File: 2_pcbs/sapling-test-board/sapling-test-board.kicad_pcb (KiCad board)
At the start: 2 copper layers, 10 parts, among them IC1 LED driver TLC59281DBQR, IC2 LED driver TLC59281DBQR, IC3 74HC138D, J1 Pin header BCS-112-L-D-PE, J2 UJC-HP-3-SMT-TR

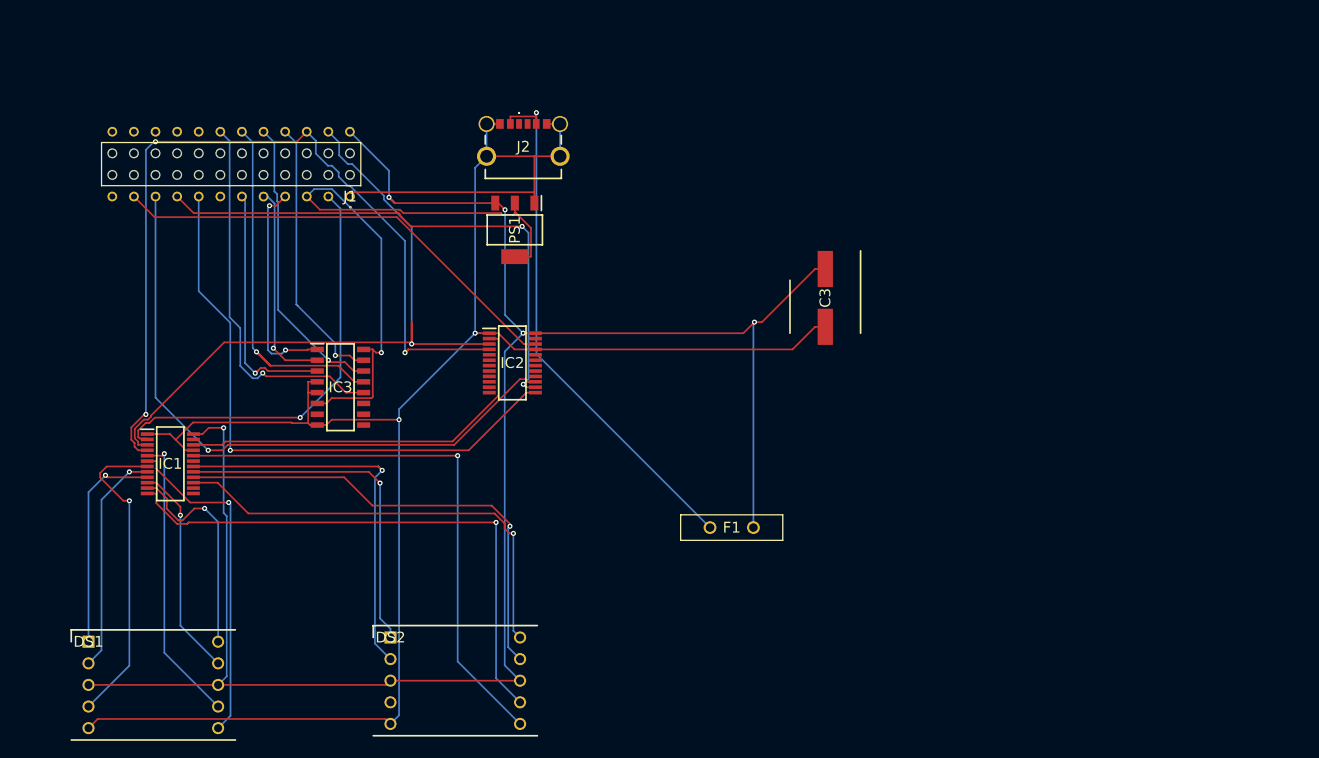
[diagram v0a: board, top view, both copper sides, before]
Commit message: Hand routed PCB
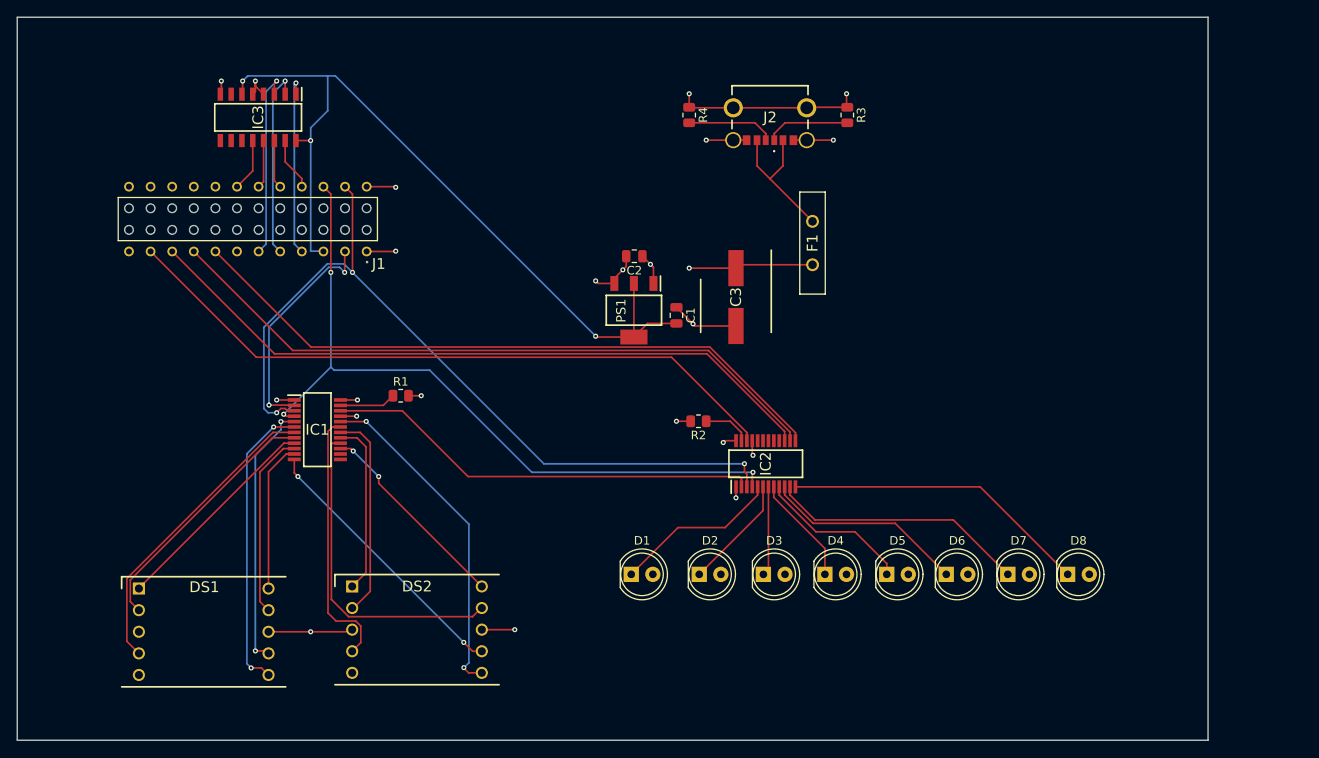
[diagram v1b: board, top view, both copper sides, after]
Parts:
- added C1: C, Capacitor_SMD:C_0805_2012Metric, F.Cu at (112.5, 55.0)
- added C2: C, Capacitor_SMD:C_0805_2012Metric, F.Cu at (107.5, 48.1)
- added D1: LED, LED_THT:LED_D5.0mm, F.Cu at (107.2, 85.5)
- added D2: LED, LED_THT:LED_D5.0mm, F.Cu at (115.2, 85.5)
- added D3: LED, LED_THT:LED_D5.0mm, F.Cu at (122.7, 85.5)
- added D4: LED, LED_THT:LED_D5.0mm, F.Cu at (130.0, 85.5)
- added D5: LED, LED_THT:LED_D5.0mm, F.Cu at (137.2, 85.5)
- added D6: LED, LED_THT:LED_D5.0mm, F.Cu at (144.2, 85.5)
- added D7: LED, LED_THT:LED_D5.0mm, F.Cu at (151.5, 85.5)
- added D8: LED, LED_THT:LED_D5.0mm, F.Cu at (158.5, 85.5)
- added R1: 6800, Resistor_SMD:R_0805_2012Metric, F.Cu at (80.1, 64.5)
- added R2: 8200, Resistor_SMD:R_0805_2012Metric, F.Cu at (115.1, 67.5)
- added R3: 5100, Resistor_SMD:R_0805_2012Metric, F.Cu at (132.6, 31.5)
- added R4: 5100, Resistor_SMD:R_0805_2012Metric, F.Cu at (114.0, 31.5)
- moved F1 38.0 mm to (128.5, 44.0), turned to -90 degrees
- moved IC3 33.2 mm to (63.3, 31.8), turned to -90 degrees
- moved IC2 32.1 mm to (123.0, 72.5), turned to 90 degrees
- moved J2 29.3 mm to (123.5, 31.5), turned to 180 degrees
- moved IC1 17.7 mm to (70.3, 68.5)
- moved PS1 16.9 mm to (107.5, 54.5)
- moved C3 10.5 mm to (119.5, 52.9)
- moved DS1 8.61 mm to (49.3, 87.2)
- moved DS2 7.50 mm to (74.4, 86.9)
- moved J1 6.75 mm to (76.1, 47.5)
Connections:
- DS2 pad 4: /7seg_3_c -> /7seg_2_c
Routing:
- net +5V: track 235.0 -> 41.6 mm, vias 5 -> 8
- net GND: track 238.3 -> 62.1 mm, vias 2 -> 15
- net Net-(J2-V-BUS_1): track 62.5 -> 17.4 mm, vias 1 -> 0
- net /Decoder-out-2: track 49.9 -> 5.66 mm, vias 1 -> 0
- net /Decoder-out-3: track 44.8 -> 6.19 mm, vias 1 -> 0
- net Net-(D8-K): track 0.00 -> 36.3 mm
- net /7seg_2_a: track 65.8 -> 32.4 mm, vias 1 -> 2
- net /7seg_2_c: track 0.00 -> 30.9 mm
- net Net-(D7-K): track 0.00 -> 30.4 mm
- net /7seg_2_g: track 53.0 -> 23.8 mm, vias 1 -> 2
- net /Decoder-out-1: track 34.7 -> 5.71 mm, vias 1 -> 0
- net /Decoder-out-0: track 32.5 -> 6.23 mm, vias 1 -> 0
- net /7seg_2_b: track 65.6 -> 39.7 mm, vias 1 -> 2
- net /led_driver_sout: track 54.4 -> 79.9 mm
- net /7seg_2_d: track 48.3 -> 24.5 mm, vias 1 -> 0
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- added copper zone on In2.Cu, net +5V
- added copper zone on In1.Cu, net GND
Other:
- board outline added: 140 x 85 mm
- copper layers 2 -> 4

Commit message: BB PCB review
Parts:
- added C4: 100nf, Capacitor_SMD:C_0805_2012Metric, F.Cu at (60.0, 24.5)
- added C5: 100nf, Capacitor_SMD:C_0805_2012Metric, F.Cu at (116.5, 72.0)
- added C6: 100nf, Capacitor_SMD:C_0805_2012Metric, F.Cu at (70.5, 61.5)
- added TP1: LED Driver 2 sout, TestPoint:TestPoint_Pad_D4.0mm, F.Cu at (104.0, 66.5)
- added TP2: +5v, TestPoint:TestPoint_Pad_D4.0mm, F.Cu at (140.5, 49.0)
- added TP3: GND, TestPoint:TestPoint_Pad_D4.0mm, F.Cu at (140.5, 40.5)
- added TP4: +3.3v, TestPoint:TestPoint_Pad_D4.0mm, F.Cu at (94.5, 34.0)
- added TP5: SIN between, TestPoint:TestPoint_Pad_D4.0mm, F.Cu at (97.5, 78.5)
- C1, C2: value C -> 500nf
- moved C2 35.7 mm to (79.5, 26.0)
- moved PS1 35.7 mm to (79.5, 32.4)
- moved C1 35.7 mm to (84.5, 33.0)
- moved C3 6.32 mm to (119.0, 46.6)
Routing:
- net +3.3V: track 97.2 -> 70.0 mm, vias 3 -> 1
- net GND: track 62.1 -> 78.4 mm
- net +5V: track 41.6 -> 48.9 mm, vias 8 -> 7
- net /led_driver_sout: track 79.9 -> 86.4 mm
- net Net-(IC1-SOUT): track 51.4 -> 57.8 mm

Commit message: Silkscreen
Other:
- board text added: "+3.3v"
- board text added: "+5v"
- board text added: "0"
- board text added: "1"
- board text added: "2"
- board text added: "3"
- board text added: "Dec in 0"
- board text added: "Dec in 1"
- board text added: "Dec in 2"
- board text added: "Dec out:"
- board text added: "GND"
- board text added: "Jye Lewis"
- board text added: "LED Drv 0"
- board text added: "LED Drv 1"
- board text added: "LED Drv 2"
- board text added: "LED Drv sout"
- board text added: "LED latch"
- board text added: "SPI Clock"
- board text added: "SPI Data"
- board text added: "Sapling test board v1.0"

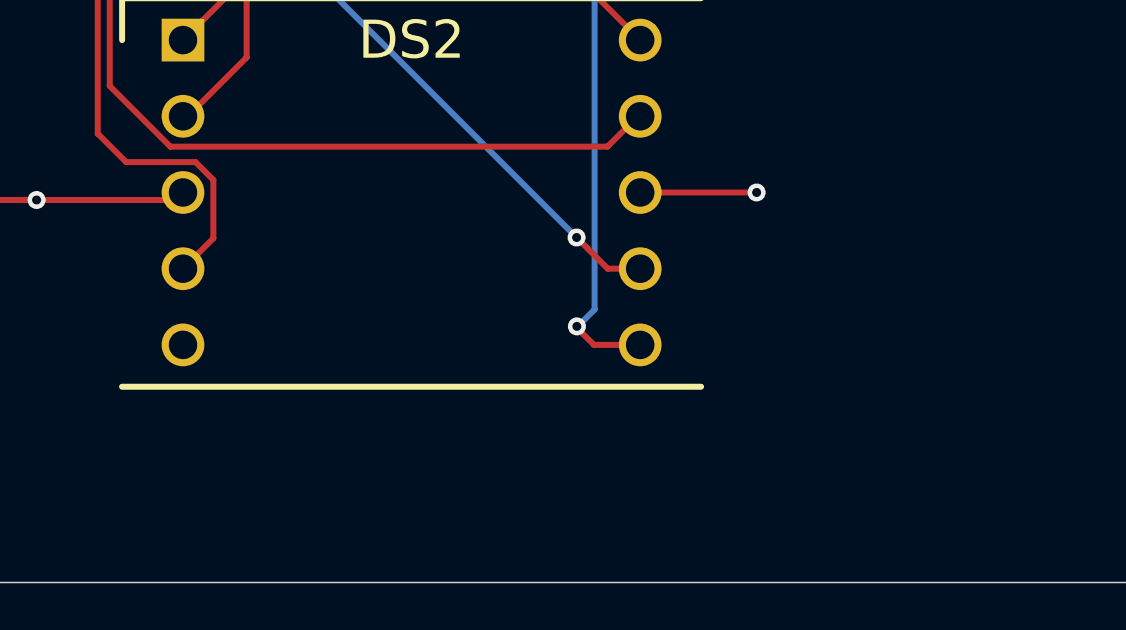
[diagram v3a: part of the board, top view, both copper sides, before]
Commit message: Test board PCB ordered
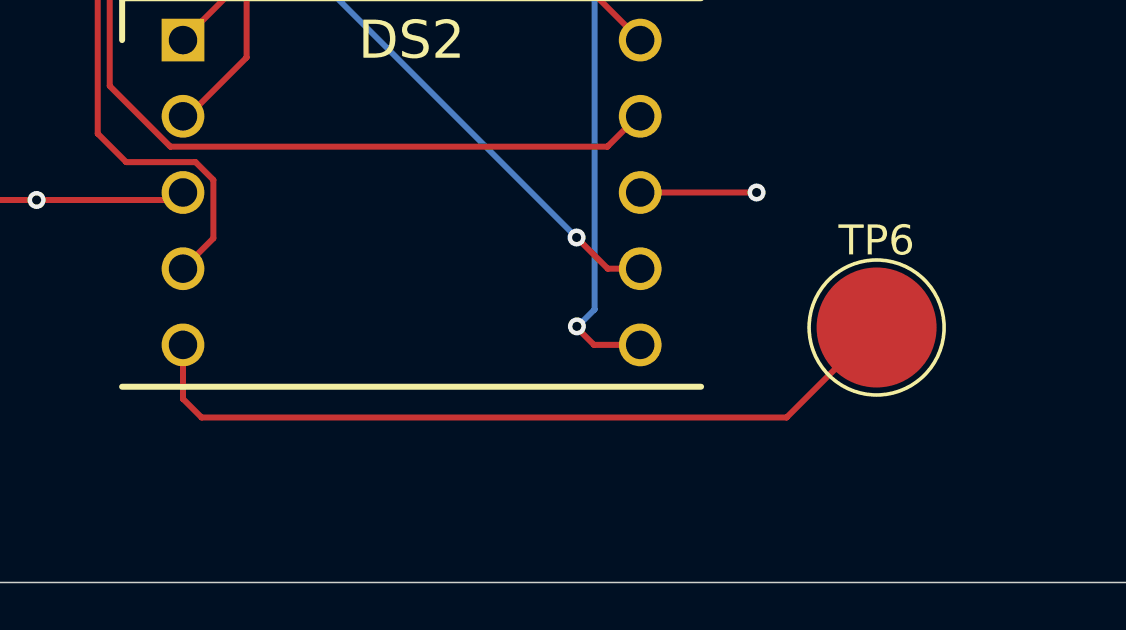
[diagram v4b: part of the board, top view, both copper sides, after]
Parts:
- added TP6: TestPoint, TestPoint:TestPoint_Pad_D4.0mm, F.Cu at (97.5, 96.5)
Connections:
- DS1 pad 5: GND -> unconnected-(DS1-CATHODE_DP-Pad5)
- DS2 pad 5: GND -> Net-(DS2-CATHODE_DP)
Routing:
- net Net-(DS2-CATHODE_DP): track 0.00 -> 26.4 mm
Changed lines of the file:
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@@
 			(plot_on_all_layers_selection 0x00000000_00000000_00000000_00000000)
 			(disableapertmacros no)
-			(usegerberextensions no)
+			(usegerberextensions yes)
 			(usegerberattributes yes)
 			(usegerberadvancedattributes yes)
@@
 			(drillshape 0)
 			(scaleselection 1)
-			(outputdirectory "")
+			(outputdirectory "output/")
 		)
 	)
@@
 			(layers "*.Cu" "*.Mask")
 			(remove_unused_layers no)
-			(net "GND")
+			(net "Net-(DS2-CATHODE_DP)")
 			(pinfunction "CATHODE_DP_5")
 			(pintype "passive")
@@
 			(layers "*.Cu" "*.Mask")
 			(remove_unused_layers no)
-			(net "GND")
+			(net "unconnected-(DS1-CATHODE_DP-Pad5)")
 			(pinfunction "CATHODE_DP_5")
-			(pintype "passive")
+			(pintype "passive+no_connect")
 		)
 		(pad "6" thru_hole circle
@@
 		)
 	)
+	(footprint "TestPoint:TestPoint_Pad_D4.0mm"
+		(layer "F.Cu")
+		(at 97.5 96.5)
+		(descr "SMD pad as test Point, diameter 4.0mm")
+		(tags "test point SMD pad")
+		(property "Reference" "TP6"
+			(at 0 -2.898 0)
+			(layer "F.SilkS")
+			(effects
+				(font
+					(size 1 1)
+					(thickness 0.15)
+				)
+			)
+		)
+		(property "Value" "TestPoint"
+			(at 0 3.1 0)
+			(layer "F.Fab")
+			(effects
+				(font
+					(size 1 1)
+					(thickness 0.15)
+				)
+			)
+		)
+		(property "Datasheet" ""
+			(at 0 0 0)
+			(unlocked yes)
+			(layer "F.Fab")
+			(hide yes)
+			(effects
+				(font
+					(size 1.27 1.27)
+					(thickness 0.15)
+				)
+			)
+		)
+		(property "Description" "test point"
+			(at 0 0 0)
+			(unlocked yes)
+			(layer "F.Fab")
+			(hide yes)
+			(effects
+				(font
+					(size 1.27 1.27)
+					(thickness 0.15)
+				)
+			)
+		)
+		(property ki_fp_filters "Pin* Test*")
+		(sheetname "/")
+		(sheetfile "sapling-test-board.kicad_sch")
+		(units
+			(unit
+				(name "A")
+				(pins "1")
+			)
+		)
+		(duplicate_pad_numbers_are_jumpers no)
+		(fp_circle
+			(center 0 0)
+			(end 0 2.25)
+			(stroke
+				(width 0.12)
+				(type solid)
+			)
+			(fill no)
+			(layer "F.SilkS")
+		)
+		(fp_circle
+			(center 0 0)
+			(end 2.5 0)
+			(stroke
+				(width 0.05)
+				(type solid)
+			)
+			(fill no)
+			(layer "F.CrtYd")
+		)
+		(fp_text user "${REFERENCE}"
+			(at 0 -2.9 0)
+			(layer "F.Fab")
+			(effects
+				(font
+					(size 1 1)
+					(thickness 0.15)
+				)
+			)
+		)
+		(pad "1" smd circle
+			(at 0 0)
+			(size 4 4)
+			(layers "F.Cu" "F.Mask")
+			(net "Net-(DS2-CATHODE_DP)")
+			(pinfunction "1_1")
+			(pintype "passive")
+		)
+		(embedded_fonts no)
+	)
 	(footprint "3-8 decoder:SOIC127P600X175-16N"
 		(layer "F.Cu")
@@
 		(net "/Decoder-out-3")
 	)
+	(segment
+		(start 74.38 97.08)
+		(end 74.38 98.88)
+		(width 0.2)
+		(layer "F.Cu")
+		(net "Net-(DS2-CATHODE_DP)")
+	)
+	(segment
+		(start 75 99.5)
+		(end 94.5 99.5)
+		(width 0.2)
+		(layer "F.Cu")
+		(net "Net-(DS2-CATHODE_DP)")
+	)
+	(segment
+		(start 94.5 99.5)
+		(end 97.5 96.5)
+		(width 0.2)
+		(layer "F.Cu")
+		(net "Net-(DS2-CATHODE_DP)")
+	)
+	(segment
+		(start 74.38 98.88)
+		(end 75 99.5)
+		(width 0.2)
+		(layer "F.Cu")
+		(net "Net-(DS2-CATHODE_DP)")
+	)
 	(zone
